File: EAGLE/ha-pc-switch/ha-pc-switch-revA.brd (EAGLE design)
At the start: 88.9 x 44.4 mm, 105 parts, among them J1 1X04_SMD_STRAIGHT_COMBO, Q1 NPN, Q2 NPN, Q3 NPN, Q4 NPN, U1 STM32C011FTSSOP20_STM-M, U2 ILD213T, U3 ILD213T, U4 TLP3123, U5 TLP3123, U7 REG1117-3.3, Y1 32.768kHz

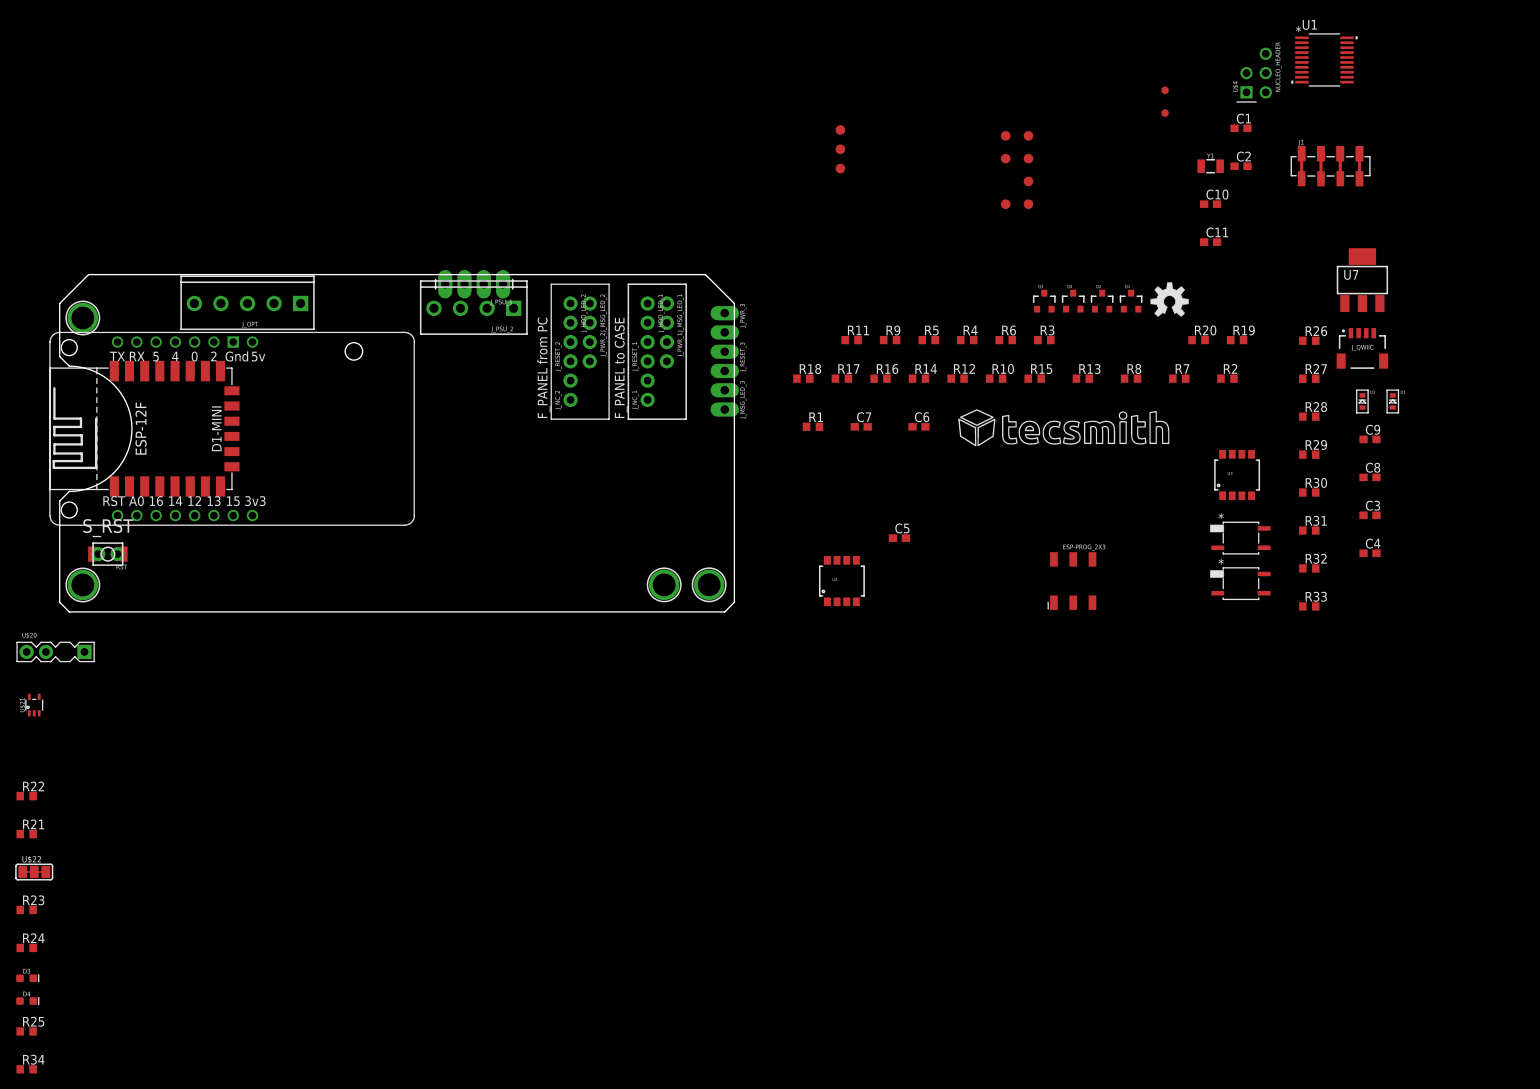
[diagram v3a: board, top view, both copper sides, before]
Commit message: pcb routed
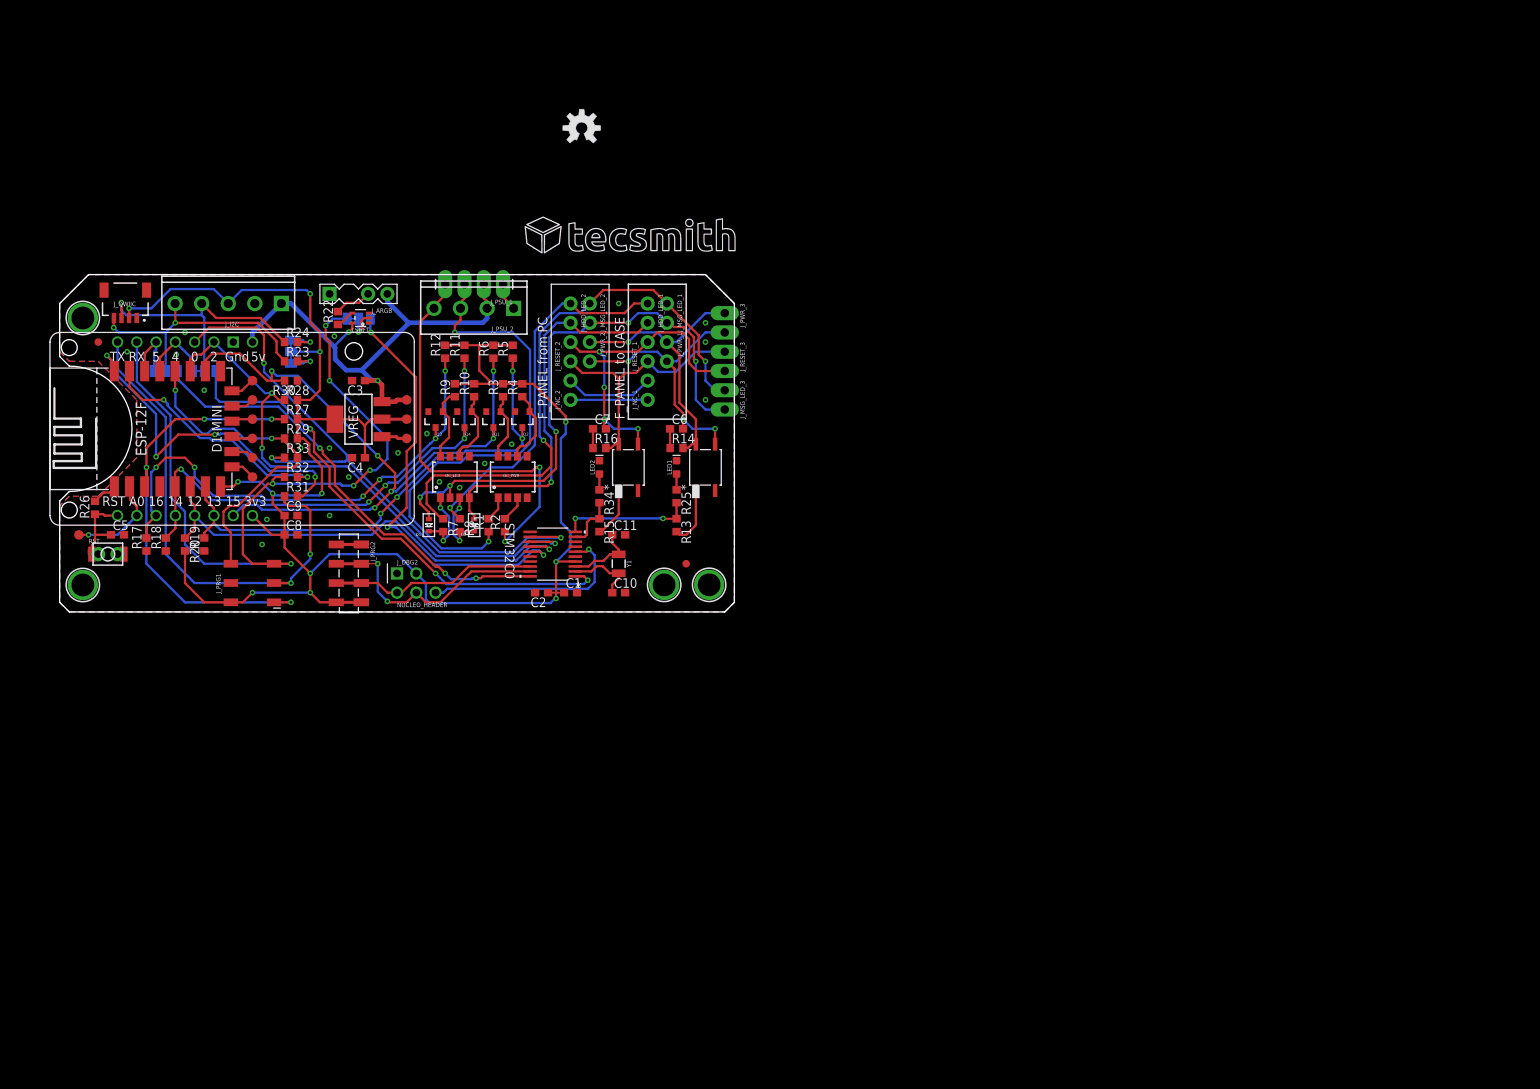
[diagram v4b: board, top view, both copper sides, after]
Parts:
- removed D3, D4: GREEN, SparkFun-LED:LED-0603
- removed ESP-PROG_2X3: (no value), SparkFun-Connectors:2X3_SMD
- removed J1: 1X04_SMD_STRAIGHT_COMBO, SparkFun-Connectors:1X04_SMD_VERTICAL_COMBO
- removed J_OPT: (no value), SparkFun-Connectors:SCREWTERMINAL-3.5MM-5
- removed R21: 220R, rcl:R0603
- removed U$20: ARGB, __temp_to_delete:ARGB
- removed U$21: 74AHCT1G125GW, ts_keyboards:SC-88A__TSSOP5__SOT353-1
- removed U$22: JUMPER-1X3-CLOSED-2, ts_jumpers:SOLDERJUMPER_CLOSEDWIRE-3-2
- removed U$4: NUCLEO_HEADER, stm32c0:NUCLEO
- removed U1: STM32C011FTSSOP20_STM-M, stm32c0:TSSOP20-M
- removed U2, U3: ILD213T, SparkFun:SO08-2
- removed U4, U5: TLP3123, __untitled:SOP4_TOS
- removed U7: REG1117-3.3, ts_custom_nick_nacks:SOT223
- added ARGB, SCL, SDA: JUMPER-1X3-CLOSED, ts_jumpers:SOLDERJUMPER_CLOSEDWIRE-3
- added I2C: JUMPER-1X3-CLOSED-2, ts_jumpers:SOLDERJUMPER_CLOSEDWIRE-3-2
- added J_ARGB: ARGB, __temp_to_delete:ARGB
- added J_DBG2: NUCLEO_HEADER, stm32c0:NUCLEO
- added J_I2C: (no value), SparkFun-Connectors:SCREWTERMINAL-3.5MM-5
- added J_PRG1: (no value), SparkFun-Connectors:2X3_SMD
- added J_PRG2: 1X04_SMD_STRAIGHT_COMBO, SparkFun-Connectors:1X04_SMD_VERTICAL_COMBO
- added LED1, LED2: GREEN, SparkFun-LED:LED-0603
- added LSHFT: 74AHCT1G125GW, ts_keyboards:SC-88A__TSSOP5__SOT353-1
- added OC_LED, OC_PWR: ILD213T, SparkFun:SO08-2
- added RL_PWR, RL_RST: TLP3123, __untitled:SOP4_TOS
- added STM32C0: STM32C011FTSSOP20_STM-M, stm32c0:TSSOP20-M
- added VREG: REG1117-3.3, ts_custom_nick_nacks:SOT223
- moved J_QWIIC 163.0 mm to (15.0, 40.0), turned to 180 degrees
- moved R26 161.5 mm to (11.0, 15.0), turned to 90 degrees
- moved U$15 144.4 mm to (11.4, 36.8)
- moved C9 142.5 mm to (36.8, 14.0)
- moved C8 142.4 mm to (36.8, 11.4)
- moved R19 138.7 mm to (25.4, 10.2), turned to 90 degrees
- moved R20 136.2 mm to (22.9, 10.2), turned to 270 degrees
- moved R33 135.6 mm to (36.8, 21.6)
- moved R30 135.0 mm to (36.8, 31.8), turned to 180 degrees
- moved R32 134.7 mm to (36.8, 19.1)
- moved TP12 134.6 mm to (8.89, 11.4)
- moved C3 134.5 mm to (45.7, 31.8), turned to 180 degrees
- moved R27 134.3 mm to (36.8, 26.7)
- moved R31 134.2 mm to (36.8, 16.5)
- moved R28 134.2 mm to (36.8, 29.2)
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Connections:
- removed net D1/SCL: D1-MINI.D1, ESP-12F.GPIO5, J_OPT.5, J_QWIIC.4, R23.1, U1.20
- removed net D2/SDA: D1-MINI.D2, ESP-12F.GPIO4, J_OPT.4, J_QWIIC.3, R24.1, U1.1
- removed net N$12: R21.2, U$21.2
- removed net RX/RGB: D1-MINI.RX, ESP-PROG_2X3.5, R21.1, R32.1, U1.15
- removed net TX: D1-MINI.TX, ESP-PROG_2X3.3, R31.1
- new net ARGB: ARGB.2, LSHFT.2
- new net RX1: ARGB.1, D1-MINI.RX, J_PRG1.5, R32.1
- new net SCL: J_I2C.5, J_QWIIC.4, R23.1, SCL.2
- new net SCL1: D1-MINI.D1, ESP-12F.GPIO5, SCL.1
- new net SCL2: SCL.3, STM32C0.20
- new net SDA: J_I2C.4, J_QWIIC.3, R24.1, SDA.2
- new net SDA1: D1-MINI.D2, ESP-12F.GPIO4, SDA.1
- new net SDA2: SDA.3, STM32C0.1
- new net TX1: D1-MINI.TX, J_PRG1.3, R31.1
- new net X_SPARE: ARGB.3, STM32C0.15
- net !X_PWR_LONG: now also STM32C0.12; no longer U1.12
- net !X_PWR_SHRT: now also STM32C0.13; no longer U1.13
- net !X_RST_SHRT: now also STM32C0.14; no longer U1.14
- net CTS2: now also STM32C0.16; no longer U1.16
- net ESP_EN: now also J_PRG1.1; no longer ESP-PROG_2X3.1
- net ESP_IO0: now also J_PRG1.6; no longer ESP-PROG_2X3.6
- net GND: now also J_ARGB.G, J_DBG2.1, J_I2C.2, J_PRG1.4, J_PRG2.1, LED1.C, LED2.C, LSHFT.1, LSHFT.3, OC_LED.5, OC_LED.7, OC_PWR.2, OC_PWR.4, OC_PWR.5, OC_PWR.7, RL_PWR.2, RL_RST.2, STM32C0.5, VREG.1; no longer D3.C, D4.C, ESP-PROG_2X3.4, J1.1, J_OPT.2, U$20.G, U$21.1, U$21.3, U$4.1, U1.5, U2.2, U2.4, U2.5, U2.7, U3.5, U3.7, U4.2, U5.2, U7.1
- net HDD_LED-: now also OC_LED.4; no longer U3.4
- net N$1: now also OC_PWR.1; no longer U2.1
- net N$10: now also STM32C0.2; no longer U1.2
- net N$11: now also STM32C0.3; no longer U1.3
- net N$13: now also OC_LED.1; no longer U3.1
- net N$17: now also LSHFT.4; no longer U$21.4
- net N$18: now also J_ARGB.D; no longer U$20.D
- net N$19: now also LED1.A; no longer D3.A
- net N$2: now also OC_PWR.3; no longer U2.3
- net N$20: now also I2C.3; no longer U$22.2
- net N$21: now also I2C.1; no longer U$22.1
- net N$25: now also LED2.A; no longer D4.A
- net N$5: now also RL_RST.1; no longer U5.1
- net N$6: now also OC_LED.3; no longer U3.3
- net N$9: now also RL_PWR.1; no longer U4.1
- net OUT1N: now also OC_PWR.8; no longer U2.8
- net OUT1N1: now also OC_LED.8; no longer U3.8
- net OUT2N: now also OC_PWR.6; no longer U2.6
- net OUT2N1: now also OC_LED.6; no longer U3.6
- net PC_ON+: now also RL_PWR.4; no longer U4.4
- net PC_ON-: now also RL_PWR.3; no longer U4.3
- net PWR_LED-: now also OC_LED.2; no longer U3.2
- net RESET: now also J_DBG2.6, STM32C0.6; no longer U$4.6, U1.6
- net RESET+: now also RL_RST.4; no longer U5.4
- net RESET-: now also RL_RST.3; no longer U5.3
- net RTS2: now also STM32C0.17; no longer U1.17
- net RX2: now also STM32C0.8; no longer U1.8
- net SWCLK: now also J_DBG2.4, J_PRG2.2, STM32C0.19; no longer J1.2, U$4.4, U1.19
- net SWDIO: now also J_DBG2.2, J_PRG2.3, STM32C0.18; no longer J1.3, U$4.2, U1.18
- net TX2: now also STM32C0.7; no longer U1.7
- net T_PWR_SWT: now also STM32C0.10; no longer U1.10
- net T_RST_SWT: now also STM32C0.9; no longer U1.9
- net VCC: now also J_ARGB.V, J_I2C.1, LSHFT.6, VREG.3; no longer C1.1, C2.1, J1.4, J_OPT.1, U$20.V, U$21.6, U$22.3, U$4.3, U1.4, U7.3
- net VDD: now also C1.1, C2.1, I2C.2, J_DBG2.3, J_I2C.3, J_PRG1.2, J_PRG2.4, STM32C0.4, VREG.2, VREG.T; no longer ESP-PROG_2X3.2, J_OPT.3, U7.2, U7.T
- net WAKE: now also STM32C0.11; no longer U1.11
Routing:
- net VDD: track 0.00 -> 245.1 mm, vias 0 -> 12
- net RX1: track 0.00 -> 105.5 mm, vias 0 -> 6
- net S_PWR_OK: track 0.00 -> 90.5 mm, vias 0 -> 6
- net !X_PWR_LONG: track 0.00 -> 81.3 mm, vias 0 -> 3
- net PWR_LED-: track 0.00 -> 76.5 mm, vias 0 -> 5
- net PWR_LED+: track 0.00 -> 76.4 mm, vias 0 -> 2
- net !X_PWR_SHRT: track 0.00 -> 75.4 mm, vias 0 -> 3
- net S_5VIN: track 0.00 -> 68.2 mm, vias 0 -> 4
- net SDA2: track 0.00 -> 67.8 mm, vias 0 -> 3
- net S_PWR_LED: track 0.00 -> 66.7 mm, vias 0 -> 6
- net TX1: track 0.00 -> 66.1 mm, vias 0 -> 2
- net VCC: track 0.00 -> 65.8 mm, vias 0 -> 2
- net PWR_OK: track 0.00 -> 65.8 mm, vias 0 -> 2
- net S_HDD_LED: track 0.00 -> 65.1 mm, vias 0 -> 5
- net !X_RST_SHRT: track 0.00 -> 61.9 mm, vias 0 -> 1
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- added copper zone on layer 1, net GND
- added copper zone on layer 16, net GND

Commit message: _
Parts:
- added J_RGB_5V: JUMPER-1X3-CLOSEDPINS, ts_jumpers:1X03_ROUND_CLOSED
- added TP4: TEST-POINT3X5, SparkFun-Connectors:PAD.03X.05
- moved U$1 39.7 mm to (90.4, 17.0), flipped to the bottom
- moved LOGO1 39.3 mm to (62.2, 27.9), flipped to the bottom
- moved U$16 35.6 mm to (90.2, 43.2)
- moved U$15 33.1 mm to (14.0, 3.81)
- moved R22 9.61 mm to (52.1, 36.8)
- moved ARGB 5.39 mm to (49.6, 36.1)
- moved LSHFT 4.74 mm to (49.5, 36.8), turned to 270 degrees
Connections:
- new net N$12: J_ARGB.V, J_RGB_5V.2, LSHFT.6
- net 5VIN: now also J_RGB_5V.1
- net VCC: now also J_RGB_5V.3; no longer J_ARGB.V, LSHFT.6
- net WAKE: now also TP4.1
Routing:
- net N$12: track 0.00 -> 9.41 mm, vias 0 -> 1
- net VDD: track 245.1 -> 254.0 mm, vias 12 -> 11
- net 5VIN: track 54.2 -> 60.8 mm
- net PWR_LED-: track 76.5 -> 82.9 mm
- net VCC: track 65.8 -> 59.5 mm, vias 2 -> 1
- net !X_RST_SHRT: track 61.9 -> 66.8 mm
- net N$18: track 4.96 -> 9.65 mm, vias 0 -> 1
- net X_SPARE: track 57.1 -> 61.4 mm
- net RX1: track 105.5 -> 102.6 mm
- net !X_PWR_LONG: track 81.3 -> 78.5 mm
- net WAKE: track 0.00 -> 2.19 mm
- net !X_PWR_SHRT: track 75.4 -> 76.9 mm
- net PWR_LED+: track 76.4 -> 77.5 mm
- net N$17: track 2.53 -> 1.54 mm
- net ARGB: track 4.62 -> 5.29 mm
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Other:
- board text added: "(c) 2024"
- board text added: "+RST-"
- board text added: "-HLED+"
- board text added: "-LED+"
- board text added: "-PLED+"
- board text added: "-PWR+"
- board text added: "-RST+"
- board text added: "3V3"
- board text added: "5V"
- board text added: "5V STBY"
- board text added: "A0"
- board text added: "DATA"
- board text added: "GND"
- board text added: "GND BLK"
- board text added: "HA PC Switch"
- board text added: "I2C"
- board text added: "OK GREY"
- board text added: "Open Source Hardware by Vino Rodrigues https://c1k.it/hapc"
- board text added: "PWR"
- board text added: "PWR RED"
- board text added: "Rev. 1.0"
- board text added: "SCL"
- board text added: "SDA"
- board text added: "STBY"
- board text added: "STBY PRPL"
- board text added: "WAKE"
